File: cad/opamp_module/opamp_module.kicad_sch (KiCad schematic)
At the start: 8 parts, among them U1 ${SIM.PARAMS}, U2 ADC101C021CIMK

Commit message: Add missing notes
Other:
- note added: "Missing: - Shielding - Input offset voltage compensation - Gain computation - actual opamp used - actual adc used - connections for MCU - voltage connections - low pass filters for input"
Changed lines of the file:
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@@
+		)
+	)
+	(text "Missing:\n- Shielding\n- Input offset voltage compensation\n- Gain computation\n- actual opamp used\n- actual adc used\n- connections for MCU\n- voltage connections\n- low pass filters for input"
+		(exclude_from_sim no)
+		(at 123.444 51.562 0)
+		(effects
+			(font
+				(size 1.27 1.27)
+			)
+			(justify left)
 		)
 	)

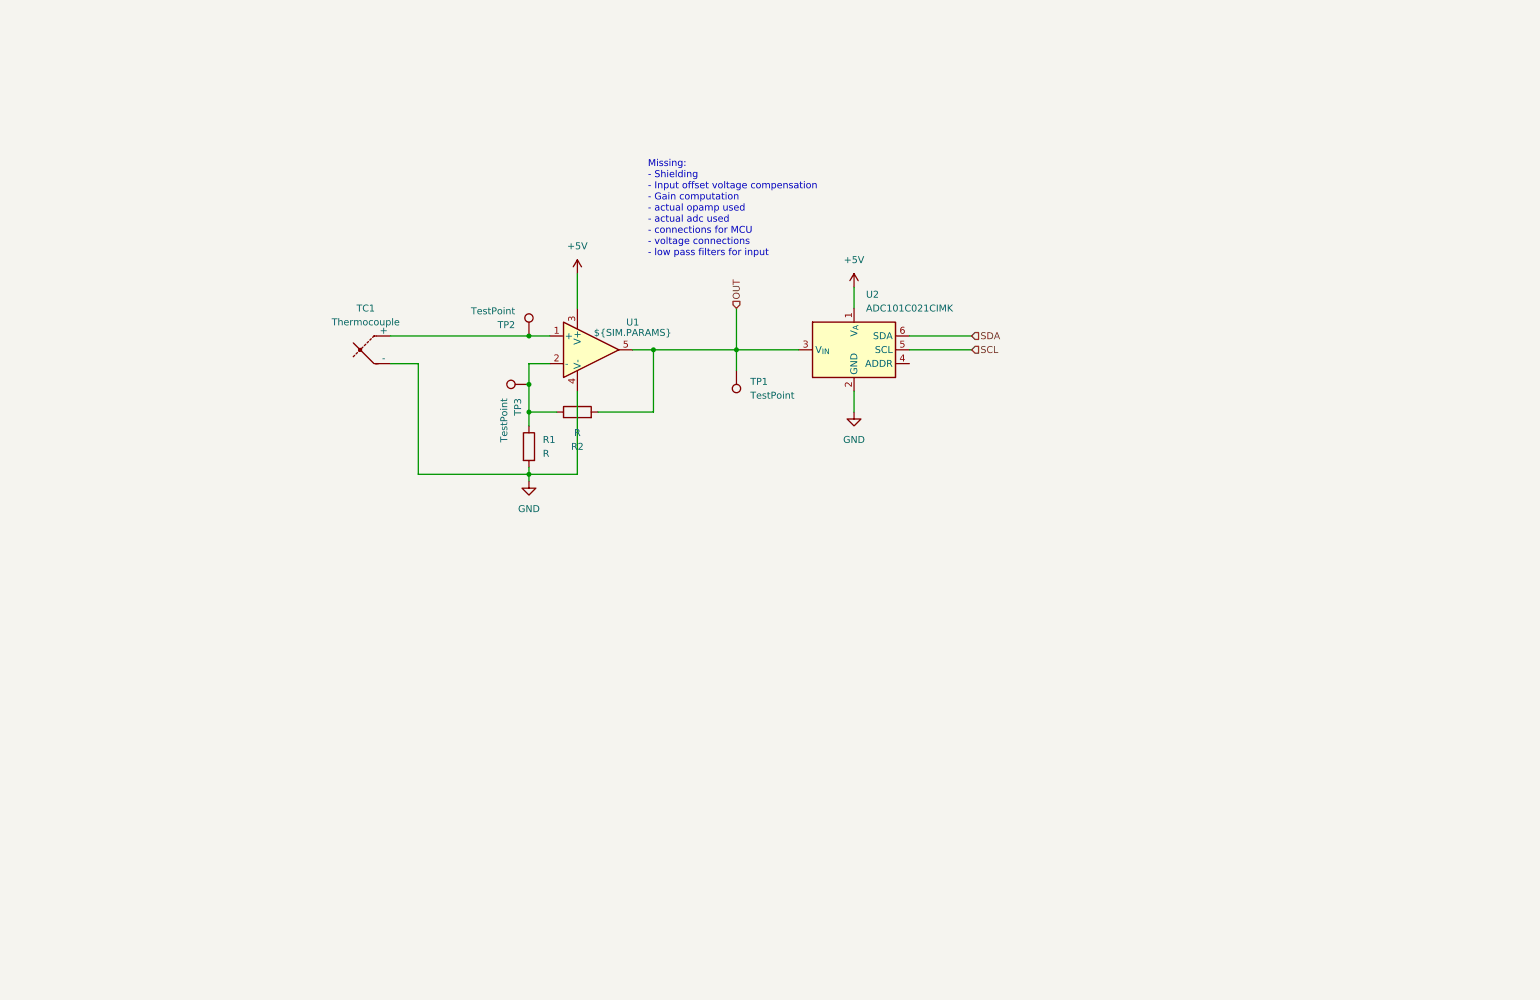
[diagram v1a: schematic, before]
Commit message: opamp module design
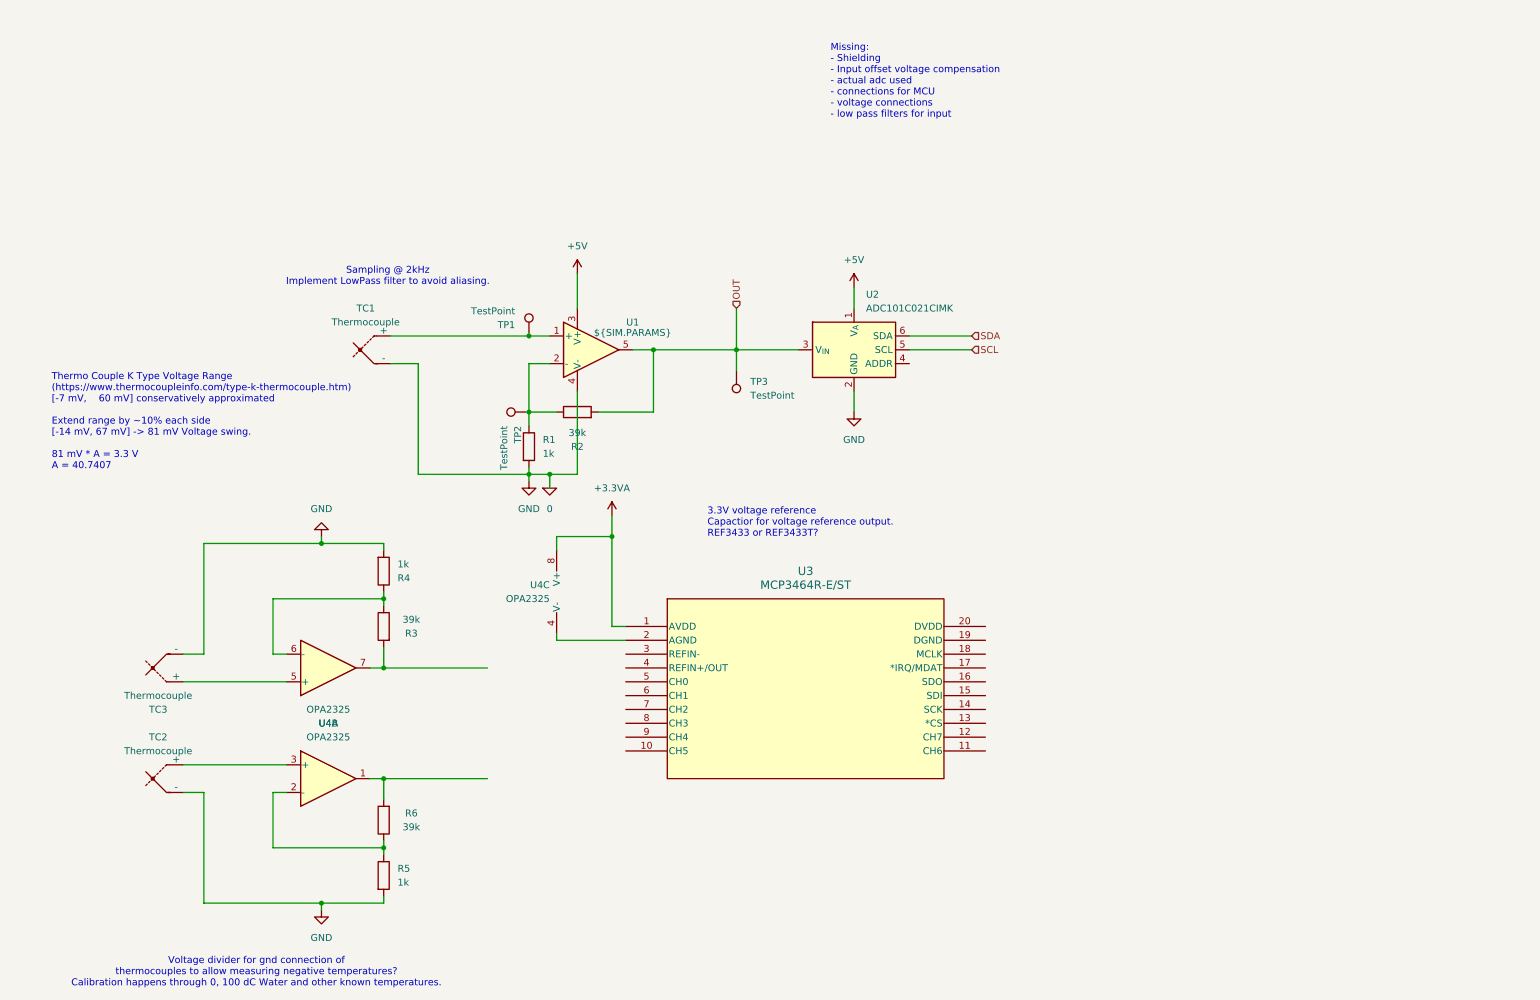
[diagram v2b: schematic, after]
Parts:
- added R3, R6: 39k, Library:MFP-25BRD52-39K, symbol Device:R
- added R4, R5: 1k, Library:MFP-25BRD52-1K, symbol Device:R
- added TC2, TC3: Thermocouple, symbol Device:Thermocouple
- added U3: MCP3464R-E/ST, symbol Library:MCP3464R-E_ST
- added U4: OPA2325, Package_SO:SOIC-8_3.9x4.9mm_P1.27mm, symbol Amplifier_Operational:OPA2325
- R1: value R -> 1k; footprint (none) -> Library:MFP-25BRD52-1K
- R2: value R -> 39k; footprint (none) -> Library:MFP-25BRD52-39K
- renumbered TP2 to TP1, TP3 to TP2, TP1 to TP3
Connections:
- net GND renamed 0
- net 0: now also R4.2, R5.2, TC2.2 (-), TC3.2 (-)
- new net: R3.1, R4.1, U4.6 (-)
- new net: R3.2, U4.7
- new net: U3.2 (AGND), U4.4 (V-)
- new net: R5.1, R6.1, U4.2 (-)
- new net: TC2.1 (+), U4.3 (+)
- new net: TC3.1 (+), U4.5 (+)
- new net: R6.2, U4.1
- new net +3.3VA: U3.1 (AVDD), U4.8 (V+)
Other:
- note added: "3.3V voltage reference Capactior for voltage reference output. REF3433 or REF3433T?"
- note added: "Missing: - Shielding - Input offset voltage compensation - actual adc used - connections for MCU - voltage connections - low pass filters for input"
- note added: "Sampling @ 2kHz Implement LowPass filter to avoid aliasing."
- note added: "Thermo Couple K Type Voltage Range (https://www.thermocoupleinfo.com/type-k-thermocouple.htm) [-7 mV, 60 mV] conservatively approximated Extend range by ~10% each side [-14 mV, 67 mV] -> 81 mV Voltage swing. 81 mV * A = 3.3 V A = 40.7407"
- note added: "Voltage divider for gnd connection of thermocouples to allow measuring negative temperatures? Calibration happens through 0, 100 dC Water and other known temperatures."
- note removed: "Missing: - Shielding - Input offset voltage compensation - Gain computation - actual opamp used - actual adc used - connections for MCU - voltage connections - low pass filters for input"
- moved on the sheet: TP2

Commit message: low pass filter
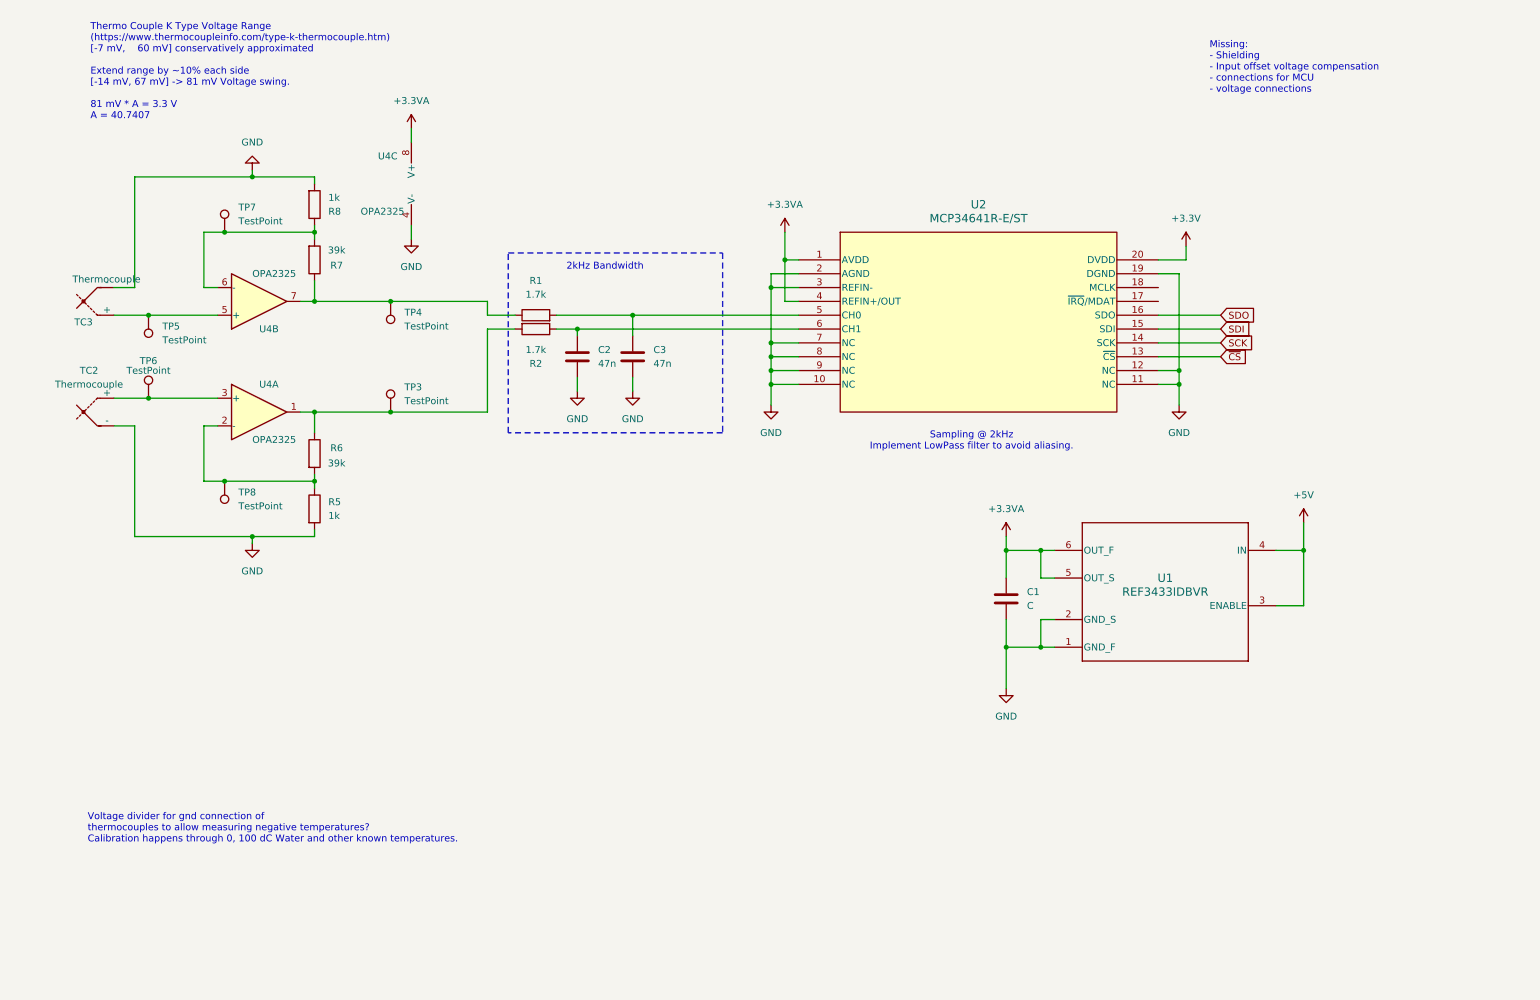
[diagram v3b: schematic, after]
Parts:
- removed R3: 39k, Library:MFP-25BRD52-39K, symbol Device:R
- removed R4: 1k, Library:MFP-25BRD52-1K, symbol Device:R
- removed TC1: Thermocouple, symbol Device:Thermocouple
- removed TP1, TP2: TestPoint, symbol Connector:TestPoint
- removed U1: ${SIM.PARAMS}, symbol Simulation_SPICE:OPAMP
- removed U2: ADC101C021CIMK, Package_TO_SOT_SMD:SOT-23-6, symbol Analog_ADC:ADC101C021CIMK
- removed U3: MCP3464R-E/ST, symbol Library:MCP3464R-E_ST
- added C1: C, symbol Device:C
- added C2, C3: 47n, symbol Device:C
- added R7: 39k, symbol Device:R
- added R8: 1k, symbol Device:R
- added TP4, TP5, TP6, TP7, TP8: TestPoint, symbol Connector:TestPoint
- added U1: REF3433IDBVR, DBV0006A_N, symbol Library:REF3433IDBVR
- added U2: MCP34641R-E/ST, TSSOP20_ST_MCH, symbol Library:MCP3461R-E/ST
- R1: value 1k -> 1.7k; footprint Library:MFP-25BRD52-1K -> (none)
- R2: value 39k -> 1.7k; footprint Library:MFP-25BRD52-39K -> (none)
- R5: footprint Library:MFP-25BRD52-1K -> (none)
- R6: footprint Library:MFP-25BRD52-39K -> (none)
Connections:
- net OUT is gone; now on an unnamed net: R2.2, TP3.1
- net +3.3VA: now also C1.1, U1.5 (OUT_S), U1.6 (OUT_F), U2.1 (AVDD), U2.4 (REFIN+/OUT)
- net +5V: now also U1.3 (ENABLE), U1.4 (IN)
- net at U4.6 (-): now also R7.2, R8.1, TP7.1
- net at U4.7: now also R1.1, R7.1, TP4.1
- net at R2.1: now also C2.1, U2.6 (CH1); no longer R1.1
- net GND: now reaches U4.4 (V-)
- net GND: now also R5.2, TC2.2 (-), TC3.2 (-), C1.2, C2.2, C3.2, R8.2, U1.1 (GND_F), U1.2 (GND_S), U2.10 (NC), U2.11 (NC), U2.12 (NC), U2.19 (DGND), U2.2 (AGND), U2.3 (REFIN-), U2.7 (NC), U2.8 (NC), U2.9 (NC)
- net at R5.1, U4.2 (-): now also R6.2, TP8.1; no longer R6.1
- net at TC2.1 (+), U4.3 (+): now also TP6.1
- net at TC3.1 (+), U4.5 (+): now also TP5.1
- net at U4.1: now also R6.1; no longer R6.2
- removed net 0: R1.2, R5.2, TC2.2 (-), TC3.2 (-)
- new net: C3.1, R1.2, U2.5 (CH0)
- new net +3.3V: U2.20 (DVDD)
- new net SCK: U2.14 (SCK)
- new net SDI: U2.15 (SDI)
- new net SDO: U2.16 (SDO)
- new net ~{CS}: U2.13 (~{CS})
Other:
- note added: "2kHz Bandwidth"
- note added: "Missing: - Shielding - Input offset voltage compensation - connections for MCU - voltage connections"
- note removed: "3.3V voltage reference Capactior for voltage reference output. REF3433 or REF3433T?"
- note removed: "Missing: - Shielding - Input offset voltage compensation - actual adc used - connections for MCU - voltage connections - low pass filters for input"
- moved on the sheet: R5, R6, TC2, TC3, TP3, U4A, U4B, U4C

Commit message: Spice based resistor selection :)
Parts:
- removed TC2: Thermocouple, symbol Device:Thermocouple
- removed U2: MCP34641R-E/ST, TSSOP20_ST_MCH, symbol Library:MCP3461R-E/ST
- added J1: Conn_02x04_Odd_Even, symbol Connector_Generic:Conn_02x04_Odd_Even
- added R11: 3M3, symbol Device:R
- added R5, R7: 9000, symbol Device:R
- added R6: 2000, symbol Device:R
- added R8: 4000, symbol Device:R
- added TH1: Thermistor, symbol Device:Thermistor
- added TP5, TP6: TestPoint, symbol Connector:TestPoint
- C2: renamed from C1; value C -> 10u
- R1: renamed from R8; value 1k -> 1M
- R2: renamed from R7; value 39k -> 32M
- R3: renamed from R6; value 39k -> 12M
- R4: renamed from R5; value 1k -> 1M
- renumbered C2 to C1, R2 to R10, R1 to R9, TC3 to TC1, TP5 to TP1, TP6 to TP2, TP7 to TP3, TP8 to TP4, TP4 to TP7, TP3 to TP8, U4 to U1, U1 to U2
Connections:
- net +3.3VA: now also R11.2, R5.1, R7.1
- net +5V: now also J1.1 (Pin_1)
- net GND: now also J1.7 (Pin_7), R6.2, R8.2; no longer R1.2, R4.2, TC1.2 (-)
- net ThemoCoupleFiltered: now reaches C3.1, R9.2
- net ThermistorFiltered: now reaches C1.1, R10.1
- net ThemoCoupleUnfiltered: now reaches R2.1, R9.1, TP7.1, U1.7
- net ThermistorUnfiltered: now reaches R10.2, R3.1, TP8.1, U1.1
- net at TP2.1, U1.3 (+): now also R11.1, TH1.2
- new net OffsetReference1: R4.2, TH1.1, TP6.1
- new net OffsetReferenceThermistor: R5.2, R6.1
- new net OffsetReferenceThermoCouple: R1.2, R7.2, R8.1, TC1.2 (-), TP5.1
- new net ThemoCoupleFiltered_{0}: J1.2 (Pin_2)
- new net ThemoCoupleFiltered_{1}: J1.4 (Pin_4)
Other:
- note added: "Filtering"
- note added: "IO"
- note added: "Measuring"
- note added: "Thermo Couple K Type Voltage Range (https://www.thermocoupleinfo.com/type-k-thermocouple.htm) [-7 mV, 60 mV] conservatively approximated Extend range for Opamp Design: [-14 mV, 77 mV]. Check opamp_spice for details on this opamp design"
- note added: "Voltage Reference"
- note removed: "Missing: - Shielding - Input offset voltage compensation - connections for MCU - voltage connections"
- note removed: "Sampling @ 2kHz Implement LowPass filter to avoid aliasing."
- note removed: "Thermo Couple K Type Voltage Range (https://www.thermocoupleinfo.com/type-k-thermocouple.htm) [-7 mV, 60 mV] conservatively approximated Extend range by ~10% each side [-14 mV, 67 mV] -> 81 mV Voltage swing. 81 mV * A = 3.3 V A = 40.7407"
- note removed: "Voltage divider for gnd connection of thermocouples to allow measuring negative temperatures? Calibration happens through 0, 100 dC Water and other known temperatures."
- moved on the sheet: C1, C2, C3, R1, R10, R2, R3, R4, R9, TC1, TP1, TP2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

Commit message: layout
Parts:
- added C4: 1u, Capacitor_SMD:C_0805_2012Metric_Pad1.18x1.45mm_HandSolder, symbol Device:C
- C1, C2, C3: footprint (none) -> Capacitor_SMD:C_0805_2012Metric_Pad1.18x1.45mm_HandSolder
- J1: footprint (none) -> Connector_PinHeader_2.54mm:PinHeader_2x04_P2.54mm_Vertical
- R1, R10, R11, R2, R3, R4, R5, R6, R7, R8, R9, TH1: footprint (none) -> Resistor_SMD:R_0805_2012Metric_Pad1.20x1.40mm_HandSolder
- TC1: footprint (none) -> Connector_PinHeader_2.54mm:PinHeader_1x02_P2.54mm_Vertical
- TP1, TP2, TP3, TP4, TP5, TP6, TP7, TP8: footprint (none) -> TestPoint:TestPoint_Pad_D2.0mm
- U2: footprint DBV0006A_N -> Library:DBV0006A_N
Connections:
- net OffsetReference1 is gone; now on net OffsetReferenceThermistor: R4.2, TH1.1, TP6.1
- net ThemoCoupleFiltered_{0} is gone; now on net GND: J1.2 (Pin_2)
- net +5V: now also C4.1
- net GND: now also C4.2; no longer J1.7 (Pin_7)
- net ThemoCoupleFiltered: now also J1.8 (Pin_8)
- net ThermistorFiltered: now also J1.7 (Pin_7)
- net ThemoCoupleFiltered_{1}: no longer names the net of J1.4 (Pin_4)
- no-connect marks 0 -> 4
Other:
- moved on the sheet: J1, R1, R11, R2, R3, R4, TC1, TH1, TP1, TP2, TP3, TP4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
